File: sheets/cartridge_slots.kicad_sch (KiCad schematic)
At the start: 3 parts, among them CN4 AXC90020, CN5 AXC90020, U33 74HC04

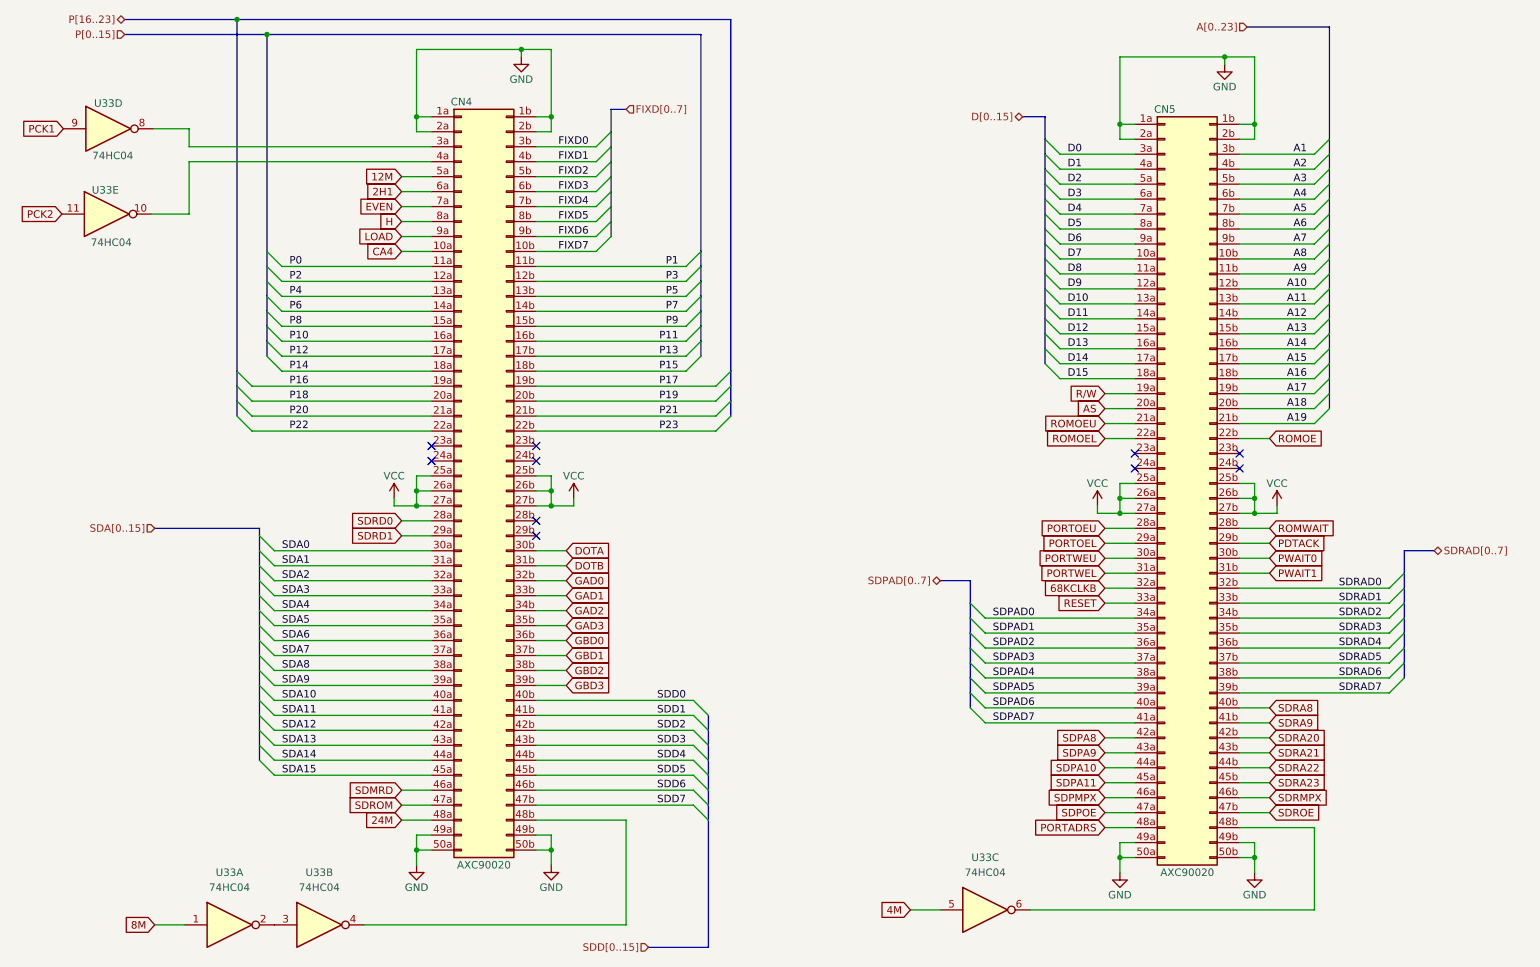
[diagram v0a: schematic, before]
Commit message: Merged in schematics from stable with footprints
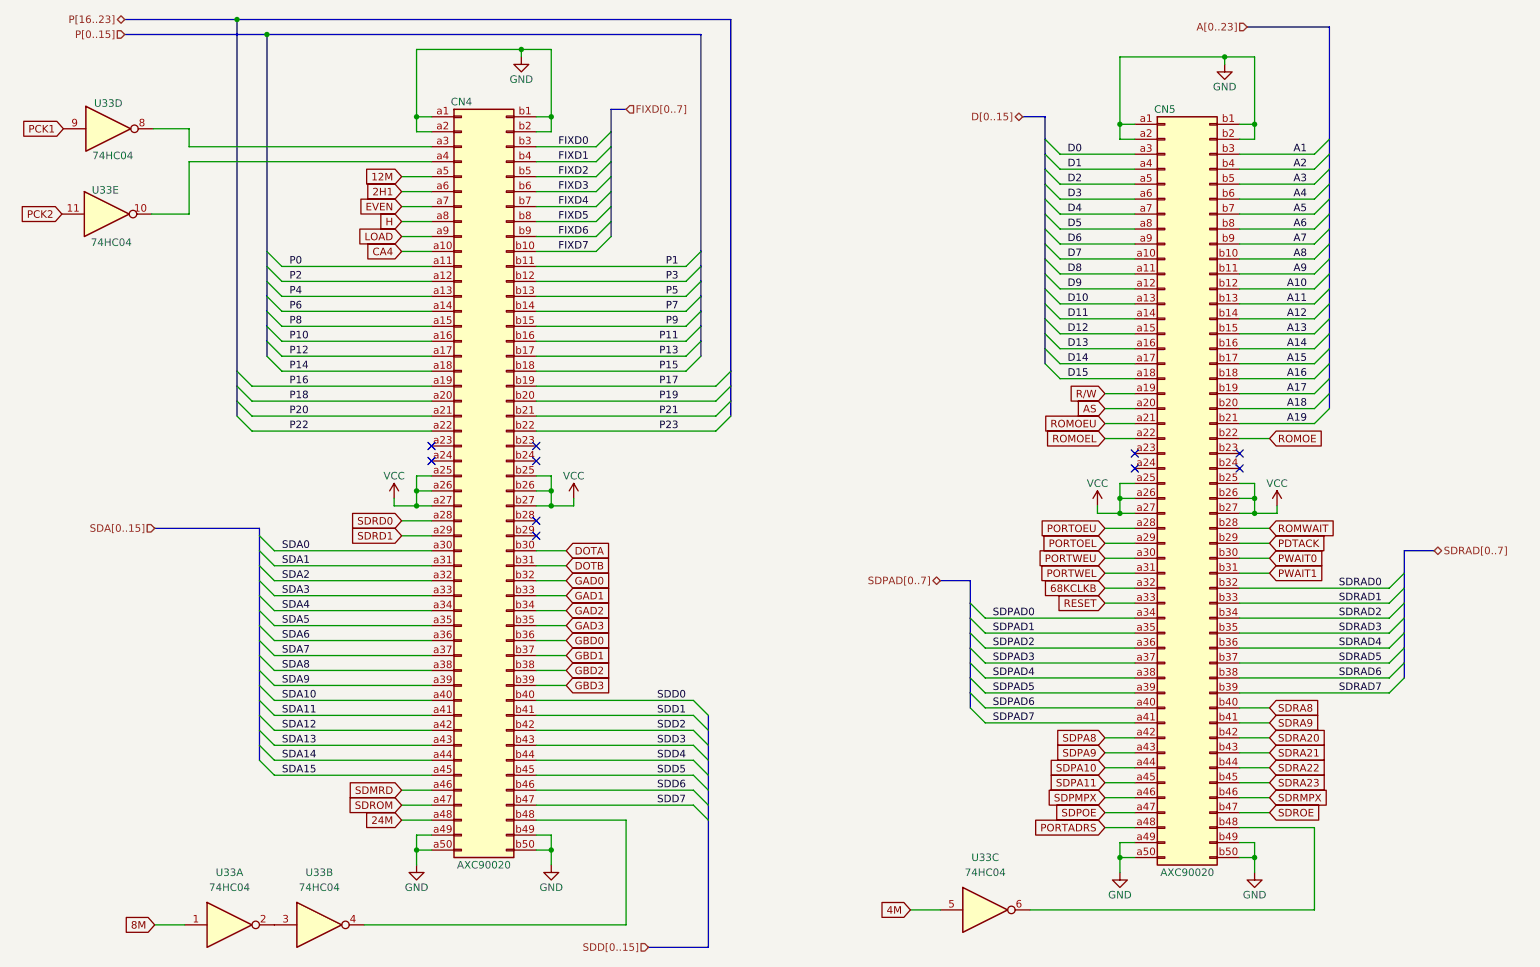
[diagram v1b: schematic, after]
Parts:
- CN4, CN5: footprint (none) -> 1_NeoGeoLibrary:AXC90020
- U33: footprint (none) -> Package_DIP:DIP-14_W7.62mm
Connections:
- net 12M: now also CN4.a5; no longer CN4.5a (Pin_5a)
- net 24M: now also CN4.a48; no longer CN4.48a (Pin_48a)
- net 2H1: now also CN4.a6; no longer CN4.6a (Pin_6a)
- net 68KCLKB: now also CN5.a32; no longer CN5.32a (Pin_32a)
- net A1: now also CN5.b3; no longer CN5.3b (Pin_3b)
- net A10: now also CN5.b12; no longer CN5.12b (Pin_12b)
- net A11: now also CN5.b13; no longer CN5.13b (Pin_13b)
- net A12: now also CN5.b14; no longer CN5.14b (Pin_14b)
- net A13: now also CN5.b15; no longer CN5.15b (Pin_15b)
- net A14: now also CN5.b16; no longer CN5.16b (Pin_16b)
- net A15: now also CN5.b17; no longer CN5.17b (Pin_17b)
- net A16: now also CN5.b18; no longer CN5.18b (Pin_18b)
- net A17: now also CN5.b19; no longer CN5.19b (Pin_19b)
- net A18: now also CN5.b20; no longer CN5.20b (Pin_20b)
- net A19: now also CN5.b21; no longer CN5.21b (Pin_21b)
- net A2: now also CN5.b4; no longer CN5.4b (Pin_4b)
- net A3: now also CN5.b5; no longer CN5.5b (Pin_5b)
- net A4: now also CN5.b6; no longer CN5.6b (Pin_6b)
- net A5: now also CN5.b7; no longer CN5.7b (Pin_7b)
- net A6: now also CN5.b8; no longer CN5.8b (Pin_8b)
- net A7: now also CN5.b9; no longer CN5.9b (Pin_9b)
- net A8: now also CN5.b10; no longer CN5.10b (Pin_10b)
- net A9: now also CN5.b11; no longer CN5.11b (Pin_11b)
- net AS: now also CN5.a20; no longer CN5.20a (Pin_20a)
- net CA4: now also CN4.a10; no longer CN4.10a (Pin_10a)
- net D0: now also CN5.a3; no longer CN5.3a (Pin_3a)
- net D1: now also CN5.a4; no longer CN5.4a (Pin_4a)
- net D10: now also CN5.a13; no longer CN5.13a (Pin_13a)
- net D11: now also CN5.a14; no longer CN5.14a (Pin_14a)
- net D12: now also CN5.a15; no longer CN5.15a (Pin_15a)
- net D13: now also CN5.a16; no longer CN5.16a (Pin_16a)
- net D14: now also CN5.a17; no longer CN5.17a (Pin_17a)
- net D15: now also CN5.a18; no longer CN5.18a (Pin_18a)
- net D2: now also CN5.a5; no longer CN5.5a (Pin_5a)
- net D3: now also CN5.a6; no longer CN5.6a (Pin_6a)
- net D4: now also CN5.a7; no longer CN5.7a (Pin_7a)
- net D5: now also CN5.a8; no longer CN5.8a (Pin_8a)
- net D6: now also CN5.a9; no longer CN5.9a (Pin_9a)
- net D7: now also CN5.a10; no longer CN5.10a (Pin_10a)
- net D8: now also CN5.a11; no longer CN5.11a (Pin_11a)
- net D9: now also CN5.a12; no longer CN5.12a (Pin_12a)
- net DOTA: now also CN4.b30; no longer CN4.30b (Pin_30b)
- net DOTB: now also CN4.b31; no longer CN4.31b (Pin_31b)
- net EVEN: now also CN4.a7; no longer CN4.7a (Pin_7a)
- net FIXD0: now also CN4.b3; no longer CN4.3b (Pin_3b)
- net FIXD1: now also CN4.b4; no longer CN4.4b (Pin_4b)
- net FIXD2: now also CN4.b5; no longer CN4.5b (Pin_5b)
- net FIXD3: now also CN4.b6; no longer CN4.6b (Pin_6b)
- net FIXD4: now also CN4.b7; no longer CN4.7b (Pin_7b)
- net FIXD5: now also CN4.b8; no longer CN4.8b (Pin_8b)
- net FIXD6: now also CN4.b9; no longer CN4.9b (Pin_9b)
- net FIXD7: now also CN4.b10; no longer CN4.10b (Pin_10b)
- net GAD0: now also CN4.b32; no longer CN4.32b (Pin_32b)
- net GAD1: now also CN4.b33; no longer CN4.33b (Pin_33b)
- net GAD2: now also CN4.b34; no longer CN4.34b (Pin_34b)
- net GAD3: now also CN4.b35; no longer CN4.35b (Pin_35b)
- net GBD0: now also CN4.b36; no longer CN4.36b (Pin_36b)
- net GBD1: now also CN4.b37; no longer CN4.37b (Pin_37b)
- net GBD2: now also CN4.b38; no longer CN4.38b (Pin_38b)
- net GBD3: now also CN4.b39; no longer CN4.39b (Pin_39b)
- net GND: now also CN4.a1, CN4.a2, CN4.a49, CN4.a50, CN4.b1, CN4.b2, CN4.b49, CN4.b50, CN5.a1, CN5.a2, CN5.a49, CN5.a50, CN5.b1, CN5.b2, CN5.b49, CN5.b50; no longer CN4.1a (Pin_1a), CN4.1b (Pin_1b), CN4.2a (Pin_2a), CN4.2b (Pin_2b), CN4.49a (Pin_49a), CN4.49b (Pin_49b), CN4.50a (Pin_50a), CN4.50b (Pin_50b), CN5.1a (Pin_1a), CN5.1b (Pin_1b), CN5.2a (Pin_2a), CN5.2b (Pin_2b), CN5.49a (Pin_49a), CN5.49b (Pin_49b), CN5.50a (Pin_50a), CN5.50b (Pin_50b)
- net H: now also CN4.a8; no longer CN4.8a (Pin_8a)
- net LOAD: now also CN4.a9; no longer CN4.9a (Pin_9a)
- net P0: now also CN4.a11; no longer CN4.11a (Pin_11a)
- net P1: now also CN4.b11; no longer CN4.11b (Pin_11b)
- net P10: now also CN4.a16; no longer CN4.16a (Pin_16a)
- net P11: now also CN4.b16; no longer CN4.16b (Pin_16b)
- net P12: now also CN4.a17; no longer CN4.17a (Pin_17a)
- net P13: now also CN4.b17; no longer CN4.17b (Pin_17b)
- net P14: now also CN4.a18; no longer CN4.18a (Pin_18a)
- net P15: now also CN4.b18; no longer CN4.18b (Pin_18b)
- net P16: now also CN4.a19; no longer CN4.19a (Pin_19a)
- net P17: now also CN4.b19; no longer CN4.19b (Pin_19b)
- net P18: now also CN4.a20; no longer CN4.20a (Pin_20a)
- net P19: now also CN4.b20; no longer CN4.20b (Pin_20b)
- net P2: now also CN4.a12; no longer CN4.12a (Pin_12a)
- net P20: now also CN4.a21; no longer CN4.21a (Pin_21a)
- net P21: now also CN4.b21; no longer CN4.21b (Pin_21b)
- net P22: now also CN4.a22; no longer CN4.22a (Pin_22a)
- net P23: now also CN4.b22; no longer CN4.22b (Pin_22b)
- net P3: now also CN4.b12; no longer CN4.12b (Pin_12b)
- net P4: now also CN4.a13; no longer CN4.13a (Pin_13a)
- net P5: now also CN4.b13; no longer CN4.13b (Pin_13b)
- net P6: now also CN4.a14; no longer CN4.14a (Pin_14a)
- net P7: now also CN4.b14; no longer CN4.14b (Pin_14b)
- net P8: now also CN4.a15; no longer CN4.15a (Pin_15a)
- net P9: now also CN4.b15; no longer CN4.15b (Pin_15b)
- net PDTACK: now also CN5.b29; no longer CN5.29b (Pin_29b)
- net PORTADRS: now also CN5.a48; no longer CN5.48a (Pin_48a)
- net PORTOEL: now also CN5.a29; no longer CN5.29a (Pin_29a)
- net PORTOEU: now also CN5.a28; no longer CN5.28a (Pin_28a)
- net PORTWEL: now also CN5.a31; no longer CN5.31a (Pin_31a)
- net PORTWEU: now also CN5.a30; no longer CN5.30a (Pin_30a)
- net PWAIT0: now also CN5.b30; no longer CN5.30b (Pin_30b)
- net PWAIT1: now also CN5.b31; no longer CN5.31b (Pin_31b)
- net RESET: now also CN5.a33; no longer CN5.33a (Pin_33a)
- net ROMOE: now also CN5.b22; no longer CN5.22b (Pin_22b)
- net ROMOEL: now also CN5.a22; no longer CN5.22a (Pin_22a)
- net ROMOEU: now also CN5.a21; no longer CN5.21a (Pin_21a)
- net ROMWAIT: now also CN5.b28; no longer CN5.28b (Pin_28b)
- net R/W: now also CN5.a19; no longer CN5.19a (Pin_19a)
- net SDA0: now also CN4.a30; no longer CN4.30a (Pin_30a)
- net SDA1: now also CN4.a31; no longer CN4.31a (Pin_31a)
- net SDA10: now also CN4.a40; no longer CN4.40a (Pin_40a)
- net SDA11: now also CN4.a41; no longer CN4.41a (Pin_41a)
- net SDA12: now also CN4.a42; no longer CN4.42a (Pin_42a)
- net SDA13: now also CN4.a43; no longer CN4.43a (Pin_43a)
- net SDA14: now also CN4.a44; no longer CN4.44a (Pin_44a)
- net SDA15: now also CN4.a45; no longer CN4.45a (Pin_45a)
- net SDA2: now also CN4.a32; no longer CN4.32a (Pin_32a)
- net SDA3: now also CN4.a33; no longer CN4.33a (Pin_33a)
- net SDA4: now also CN4.a34; no longer CN4.34a (Pin_34a)
- net SDA5: now also CN4.a35; no longer CN4.35a (Pin_35a)
- net SDA6: now also CN4.a36; no longer CN4.36a (Pin_36a)
- net SDA7: now also CN4.a37; no longer CN4.37a (Pin_37a)
- net SDA8: now also CN4.a38; no longer CN4.38a (Pin_38a)
- net SDA9: now also CN4.a39; no longer CN4.39a (Pin_39a)
- net SDD0: now also CN4.b40; no longer CN4.40b (Pin_40b)
- net SDD1: now also CN4.b41; no longer CN4.41b (Pin_41b)
- net SDD2: now also CN4.b42; no longer CN4.42b (Pin_42b)
- net SDD3: now also CN4.b43; no longer CN4.43b (Pin_43b)
- net SDD4: now also CN4.b44; no longer CN4.44b (Pin_44b)
- net SDD5: now also CN4.b45; no longer CN4.45b (Pin_45b)
- net SDD6: now also CN4.b46; no longer CN4.46b (Pin_46b)
- net SDD7: now also CN4.b47; no longer CN4.47b (Pin_47b)
- net SDMRD: now also CN4.a46; no longer CN4.46a (Pin_46a)
- net SDPA10: now also CN5.a44; no longer CN5.44a (Pin_44a)
- net SDPA11: now also CN5.a45; no longer CN5.45a (Pin_45a)
- net SDPA8: now also CN5.a42; no longer CN5.42a (Pin_42a)
- net SDPA9: now also CN5.a43; no longer CN5.43a (Pin_43a)
- net SDPAD0: now also CN5.a34; no longer CN5.34a (Pin_34a)
- net SDPAD1: now also CN5.a35; no longer CN5.35a (Pin_35a)
- net SDPAD2: now also CN5.a36; no longer CN5.36a (Pin_36a)
- net SDPAD3: now also CN5.a37; no longer CN5.37a (Pin_37a)
- net SDPAD4: now also CN5.a38; no longer CN5.38a (Pin_38a)
- net SDPAD5: now also CN5.a39; no longer CN5.39a (Pin_39a)
- net SDPAD6: now also CN5.a40; no longer CN5.40a (Pin_40a)
- net SDPAD7: now also CN5.a41; no longer CN5.41a (Pin_41a)
- net SDPMPX: now also CN5.a46; no longer CN5.46a (Pin_46a)
- net SDPOE: now also CN5.a47; no longer CN5.47a (Pin_47a)
- net SDRA20: now also CN5.b42; no longer CN5.42b (Pin_42b)
- net SDRA21: now also CN5.b43; no longer CN5.43b (Pin_43b)
- net SDRA22: now also CN5.b44; no longer CN5.44b (Pin_44b)
- net SDRA23: now also CN5.b45; no longer CN5.45b (Pin_45b)
- net SDRA8: now also CN5.b40; no longer CN5.40b (Pin_40b)
- net SDRA9: now also CN5.b41; no longer CN5.41b (Pin_41b)
- net SDRAD0: now also CN5.b32; no longer CN5.32b (Pin_32b)
- net SDRAD1: now also CN5.b33; no longer CN5.33b (Pin_33b)
- net SDRAD2: now also CN5.b34; no longer CN5.34b (Pin_34b)
- net SDRAD3: now also CN5.b35; no longer CN5.35b (Pin_35b)
- net SDRAD4: now also CN5.b36; no longer CN5.36b (Pin_36b)
- net SDRAD5: now also CN5.b37; no longer CN5.37b (Pin_37b)
- net SDRAD6: now also CN5.b38; no longer CN5.38b (Pin_38b)
- net SDRAD7: now also CN5.b39; no longer CN5.39b (Pin_39b)
- net SDRD0: now also CN4.a28; no longer CN4.28a (Pin_28a)
- net SDRD1: now also CN4.a29; no longer CN4.29a (Pin_29a)
- net SDRMPX: now also CN5.b46; no longer CN5.46b (Pin_46b)
- net SDROE: now also CN5.b47; no longer CN5.47b (Pin_47b)
- net SDROM: now also CN4.a47; no longer CN4.47a (Pin_47a)
- net VCC: now also CN4.a25, CN4.a26, CN4.a27, CN4.b25, CN4.b26, CN4.b27, CN5.a25, CN5.a26, CN5.a27, CN5.b25, CN5.b26, CN5.b27; no longer CN4.25a (Pin_25a), CN4.25b (Pin_25b), CN4.26a (Pin_26a), CN4.26b (Pin_26b), CN4.27a (Pin_27a), CN4.27b (Pin_27b), CN5.25a (Pin_25a), CN5.25b (Pin_25b), CN5.26a (Pin_26a), CN5.26b (Pin_26b), CN5.27a (Pin_27a), CN5.27b (Pin_27b)
- net at U33.4: now also CN4.b48; no longer CN4.48b (Pin_48b)
- net at U33.6: now also CN5.b48; no longer CN5.48b (Pin_48b)
- net at U33.10: now also CN4.a4; no longer CN4.4a (Pin_4a)
- net at U33.8: now also CN4.a3; no longer CN4.3a (Pin_3a)

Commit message: FIX 74AS04 and 74HC04
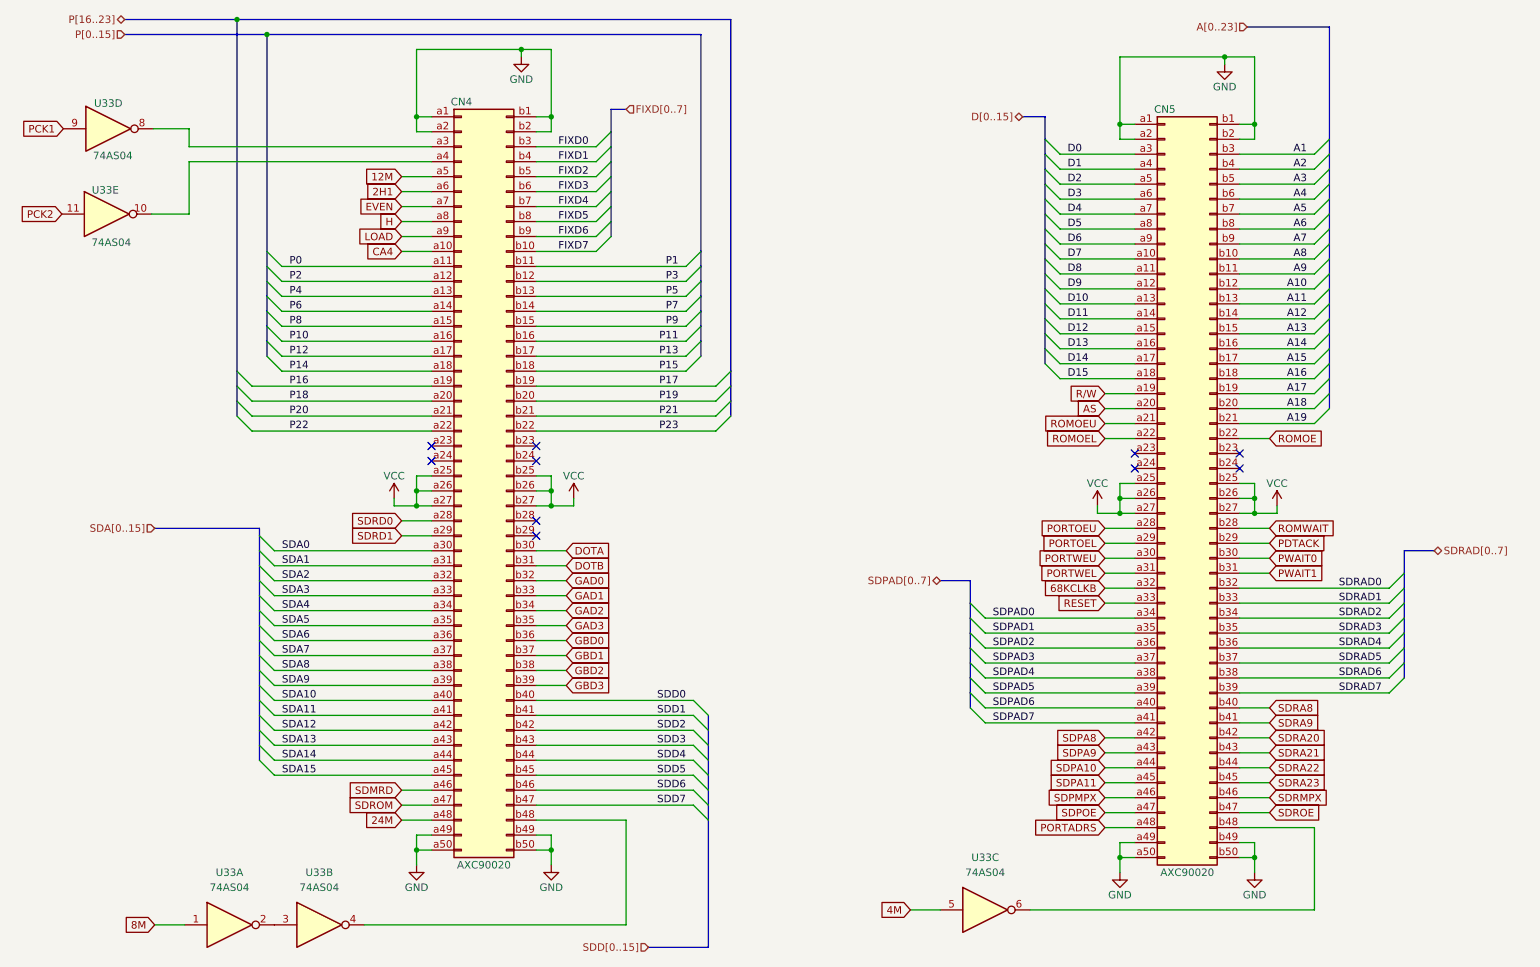
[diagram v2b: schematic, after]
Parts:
- U33: value 74HC04 -> 74AS04
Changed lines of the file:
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@@
     (in_bom yes) (on_board yes) (fields_autoplaced)
     (property "Reference" "U33" (id 0) (at 129.54 196.85 0))
-    (property "Value" "74HC04" (id 1) (at 129.54 199.39 0))
+    (property "Value" "74AS04" (id 1) (at 129.54 199.39 0))
     (property "Footprint" "Package_DIP:DIP-14_W7.62mm" (id 2) (at 129.54 205.74 0)
       (effects (font (size 1.27 1.27)) hide)
@@
     (in_bom yes) (on_board yes) (fields_autoplaced)
     (property "Reference" "U33" (id 0) (at 114.3 196.85 0))
-    (property "Value" "74HC04" (id 1) (at 114.3 199.39 0))
+    (property "Value" "74AS04" (id 1) (at 114.3 199.39 0))
     (property "Footprint" "Package_DIP:DIP-14_W7.62mm" (id 2) (at 114.3 205.74 0)
       (effects (font (size 1.27 1.27)) hide)
@@
     (in_bom yes) (on_board yes)
     (property "Reference" "U33" (id 0) (at 93.218 81.026 0))
-    (property "Value" "74HC04" (id 1) (at 94.234 89.916 0))
+    (property "Value" "74AS04" (id 1) (at 94.234 89.916 0))
     (property "Footprint" "Package_DIP:DIP-14_W7.62mm" (id 2) (at 93.472 85.09 0)
       (effects (font (size 1.27 1.27)) hide)
@@
     (in_bom yes) (on_board yes) (fields_autoplaced)
     (property "Reference" "U33" (id 0) (at 242.57 194.31 0))
-    (property "Value" "74HC04" (id 1) (at 242.57 196.85 0))
+    (property "Value" "74AS04" (id 1) (at 242.57 196.85 0))
     (property "Footprint" "Package_DIP:DIP-14_W7.62mm" (id 2) (at 242.57 203.2 0)
       (effects (font (size 1.27 1.27)) hide)
@@
     (in_bom yes) (on_board yes)
     (property "Reference" "U33" (id 0) (at 93.726 66.294 0))
-    (property "Value" "74HC04" (id 1) (at 94.488 75.184 0))
+    (property "Value" "74AS04" (id 1) (at 94.488 75.184 0))
     (property "Footprint" "Package_DIP:DIP-14_W7.62mm" (id 2) (at 93.726 70.612 0)
       (effects (font (size 1.27 1.27)) hide)

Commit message: Renamed SDD[0..15] to SDD[0..7]
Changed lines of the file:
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@@
     (effects (font (size 1.27 1.27)) (justify right))
   )
-  (hierarchical_label "SDD[0..15]" (shape input) (at 185.42 209.55 180)
+  (hierarchical_label "SDD[0..7]" (shape input) (at 185.42 209.55 180)
     (effects (font (size 1.27 1.27)) (justify right))
   )

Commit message: Sync footprints from Nightly Build
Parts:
- CN4, CN5: footprint 1_NeoGeoLibrary:AXC90020 -> 1_NeoGeoLibrary:CN4-5
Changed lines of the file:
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@@
     (property "Reference" "CN5" (id 0) (at 273.05 67.31 0))
     (property "Value" "AXC90020" (id 1) (at 276.86 196.85 0))
-    (property "Footprint" "1_NeoGeoLibrary:AXC90020" (id 2) (at 273.05 118.11 0)
+    (property "Footprint" "1_NeoGeoLibrary:CN4-5" (id 2) (at 273.05 118.11 0)
       (effects (font (size 1.27 1.27)) hide)
     )
@@
     (property "Reference" "CN4" (id 0) (at 153.67 66.04 0))
     (property "Value" "AXC90020" (id 1) (at 157.48 195.58 0))
-    (property "Footprint" "1_NeoGeoLibrary:AXC90020" (id 2) (at 153.67 116.84 0)
+    (property "Footprint" "1_NeoGeoLibrary:CN4-5" (id 2) (at 153.67 116.84 0)
       (effects (font (size 1.27 1.27)) hide)
     )

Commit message: Schematics Footprint updates
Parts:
- U33: footprint Package_DIP:DIP-14_W7.62mm -> 1_NeoGeoLibrary:DIP-14_W7.62mm
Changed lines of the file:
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@@
       (effects (font (size 1.27 1.27)))
     )
-    (property "Footprint" "Package_DIP:DIP-14_W7.62mm" (at 129.54 205.74 0)
+    (property "Footprint" "1_NeoGeoLibrary:DIP-14_W7.62mm" (at 129.54 205.74 0)
       (effects (font (size 1.27 1.27)) hide)
     )
@@
       (effects (font (size 1.27 1.27)))
     )
-    (property "Footprint" "Package_DIP:DIP-14_W7.62mm" (at 114.3 205.74 0)
+    (property "Footprint" "1_NeoGeoLibrary:DIP-14_W7.62mm" (at 114.3 205.74 0)
       (effects (font (size 1.27 1.27)) hide)
     )
@@
       (effects (font (size 1.27 1.27)))
     )
-    (property "Footprint" "Package_DIP:DIP-14_W7.62mm" (at 93.472 85.09 0)
+    (property "Footprint" "1_NeoGeoLibrary:DIP-14_W7.62mm" (at 93.472 85.09 0)
       (effects (font (size 1.27 1.27)) hide)
     )
@@
       (effects (font (size 1.27 1.27)))
     )
-    (property "Footprint" "Package_DIP:DIP-14_W7.62mm" (at 242.57 203.2 0)
+    (property "Footprint" "1_NeoGeoLibrary:DIP-14_W7.62mm" (at 242.57 203.2 0)
       (effects (font (size 1.27 1.27)) hide)
     )
@@
       (effects (font (size 1.27 1.27)))
     )
-    (property "Footprint" "Package_DIP:DIP-14_W7.62mm" (at 93.726 70.612 0)
-      (effects (font (size 1.27 1.27)) hide)
-    )
+    (property "Footprint" "1_NeoGeoLibrary:DIP-14_W7.62mm" (at 93.726 70.612 0)
+      (effects (font (size 1.27 1.27)) hide)
+    )

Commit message: Some tweaks
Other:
- company: (none) -> SNK
- title: (none) -> NeoGeo AES
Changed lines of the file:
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@@
 (kicad_sch (version 20230121) (generator eeschema)
   (paper "A3")
+  (title_block
+    (title "NeoGeo AES")
+    (date "2023-08-19")
+    (rev "3.5")
+    (company "SNK")
+    (comment 3 "https://github.com/Board-Folk")
+    (comment 4 "Recreated By The Board Folk Team")
+  )
     (symbol "74xx:74HC04" (in_bom yes) (on_board yes)
       (property "Reference" "U" (at 0 1.27 0)
